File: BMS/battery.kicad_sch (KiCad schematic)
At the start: 18 parts

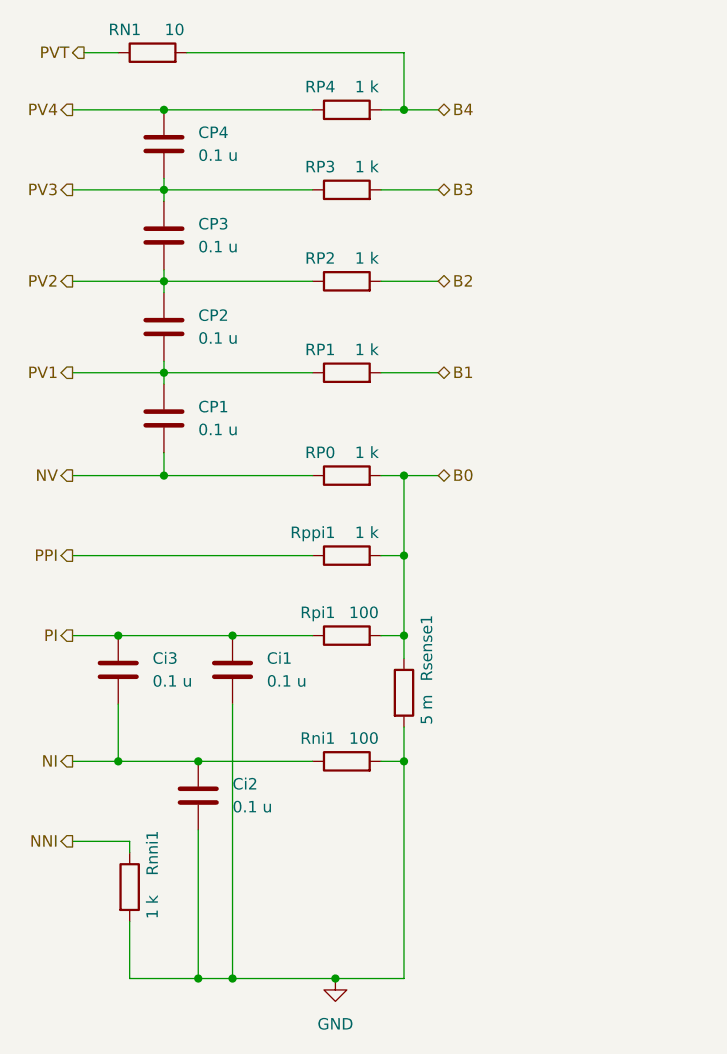
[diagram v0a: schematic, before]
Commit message: DCDC fix unavailable parts, BMS redesign, handle fix, rearrange top half
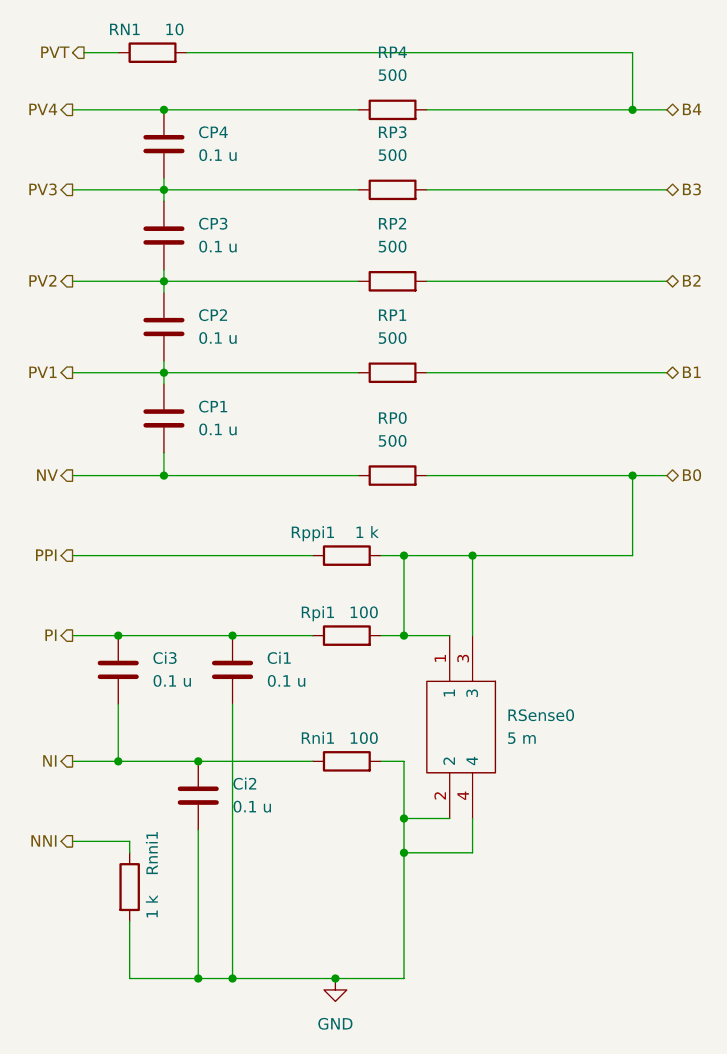
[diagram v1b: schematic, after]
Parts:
- removed Rsense1: 5 m, symbol Device:R
- added RSense0: 5 m, Y14880R00500B9R, symbol Local:Y14880R00500B9R
- CP1, CP2, CP3, CP4, Ci1, Ci2, Ci3: Manufacturer_Part_Number (none) -> KAM15AR71H104KT
- RN1: Manufacturer_Part_Number (none) -> ERJ-U0XF10R0Y
- RP0, RP1, RP2, RP3, RP4: value 1 k -> 500; footprint Resistor_SMD:R_0402_1005Metric -> Resistor_SMD:R_1206_3216Metric; Manufacturer_Part_Number (none) -> MCA12060D5000BP500
- Rni1, Rpi1: footprint (none) -> Resistor_SMD:R_0603_1608Metric; Manufacturer_Part_Number (none) -> APC0603T100RZ
- Rnni1, Rppi1: Manufacturer_Part_Number (none) -> 71-PTN0402Y5000BST1
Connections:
- net B0: now also RSense0.1, RSense0.3
- net GND: now also RSense0.2, RSense0.4
